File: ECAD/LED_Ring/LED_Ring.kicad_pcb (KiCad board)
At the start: 2 copper layers, 68.1 x 55.2 mm, 25 parts

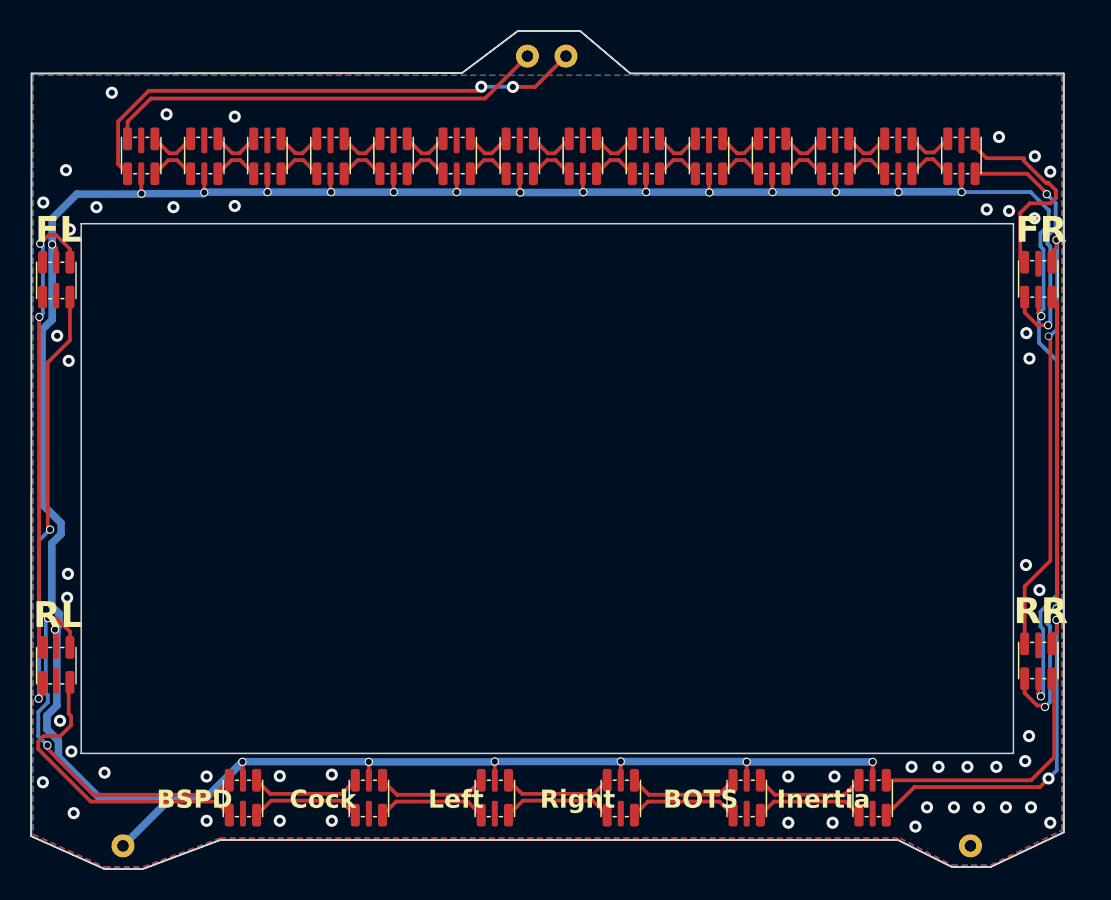
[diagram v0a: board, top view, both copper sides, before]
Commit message: switch to ribbon cable pcb interconnect
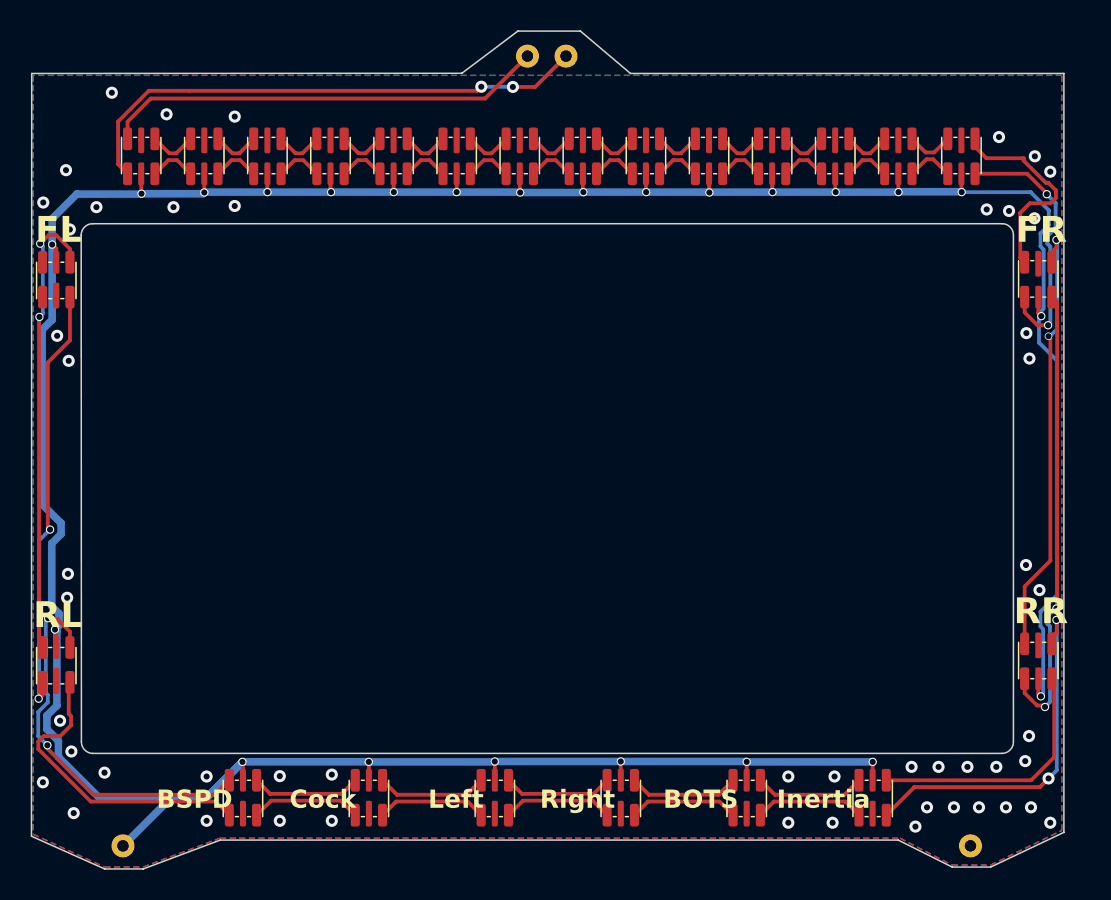
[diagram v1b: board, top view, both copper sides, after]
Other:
- outline, holes or cut-outs redrawn
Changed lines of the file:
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@@
       (net 6 "+5V") (pinfunction "VCC") (pintype "input") (thermal_bridge_angle 45))
   )
-  (gr_line (start 79.994 11.938) (end 51.419 11.938)
+  (gr_line (start 15.224 22.606) (end 15.24 55.991168)
     (stroke (width 0.1) (type default)) (layer "Edge.Cuts"))
-  (gr_line (start 75.168 64.262) (end 79.994 61.976)
+  (gr_arc (start 15.224 22.606) (mid 15.452861 22.061498) (end 16.002 21.844)
     (stroke (width 0.1) (type default)) (layer "Edge.Cuts"))
-  (gr_line (start 15.224 21.844) (end 15.224 56.769)
+  (gr_line (start 75.946 21.844) (end 16.002 21.844)
     (stroke (width 0.1) (type default)) (layer "Edge.Cuts"))
-  (gr_line (start 48.117 9.144) (end 43.9935 9.144)
+  (gr_line (start 76.692168 56.007) (end 76.692 22.606)
     (stroke (width 0.1) (type default)) (layer "Edge.Cuts"))
-  (gr_line (start 43.9935 9.144) (end 40.3025 11.924)
+  (gr_arc (start 76.692168 56.007) (mid 76.474562 56.540247) (end 75.946 56.769)
     (stroke (width 0.1) (type default)) (layer "Edge.Cuts"))
-  (gr_line (start 76.692 21.844) (end 15.224 21.844)
+  (gr_line (start 15.986 56.769) (end 75.946 56.769)
     (stroke (width 0.1) (type default)) (layer "Edge.Cuts"))
-  (gr_line (start 24.368 62.484) (end 69.072 62.484)
+  (gr_arc (start 75.946 21.844) (mid 76.479189 22.068175) (end 76.692 22.606)
     (stroke (width 0.1) (type default)) (layer "Edge.Cuts"))
-  (gr_line (start 79.994 61.976) (end 79.994 11.938)
-    (stroke (width 0.1) (type default)) (layer "Edge.Cuts"))
-  (gr_line (start 76.692 56.769) (end 76.692 21.844)
-    (stroke (width 0.1) (type default)) (layer "Edge.Cuts"))
-  (gr_line (start 16.748 64.389) (end 19.288 64.389)
-    (stroke (width 0.1) (type default)) (layer "Edge.Cuts"))
-  (gr_line (start 19.288 64.389) (end 24.368 62.484)
-    (stroke (width 0.1) (type default)) (layer "Edge.Cuts"))
-  (gr_line (start 15.224 56.769) (end 76.692 56.769)
-    (stroke (width 0.1) (type default)) (layer "Edge.Cuts"))
-  (gr_line (start 11.922 62.23) (end 16.748 64.389)
-    (stroke (width 0.1) (type default)) (layer "Edge.Cuts"))
-  (gr_line (start 51.419 11.938) (end 48.117 9.144)
-    (stroke (width 0.1) (type default)) (layer "Edge.Cuts"))
-  (gr_line (start 40.3025 11.924) (end 11.938 11.938)
-    (stroke (width 0.1) (type default)) (layer "Edge.Cuts"))
-  (gr_line (start 11.938 11.938) (end 11.922 62.23)
-    (stroke (width 0.1) (type default)) (layer "Edge.Cuts"))
-  (gr_line (start 72.628 64.262) (end 75.168 64.262)
-    (stroke (width 0.1) (type default)) (layer "Edge.Cuts"))
-  (gr_line (start 69.072 62.484) (end 72.628 64.262)
+  (gr_arc (start 15.986 56.769) (mid 15.45183 56.534658) (end 15.24 55.991168)
     (stroke (width 0.1) (type default)) (layer "Edge.Cuts"))
   (gr_line (start 78.8 67.07) (end 139.58 67.07)
